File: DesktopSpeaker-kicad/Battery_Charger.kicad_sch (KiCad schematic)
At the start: 22 parts, among them J5 1S_PACK_3PIN, Q100 2N7002, SW100 WAKE_QON, SW101 BAT_DISCONNECT, U4 BQ25895RTWR

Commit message: Checkpoint isolated BQ25792/TPS25730D/TPS2116 candidates, Q100 metadata and tool wrappers
Co-Authored-By: Claude Sonnet 5.5 <noreply@anthropic.com>
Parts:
- Q100: LCSC (none) -> C65189; MPN (none) -> 2N7002,215; Manufacturer (none) -> Nexperia
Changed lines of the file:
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@@
 (wire (pts (xy 181.61 217.17) (xy 217.83 217.17)) (stroke (width 0) (type default)))
 (wire (pts (xy 217.83 217.17) (xy 217.83 205.42)) (stroke (width 0) (type default)))
-(symbol (lib_id "2N7002:2N7002") (at 173.99 232.41 0) (unit 1) (exclude_from_sim no) (in_bom yes) (on_board yes) (dnp no) (property "Reference" "Q100" (at 182.88 231.14 0) (effects (font (size 1.27 1.27)) (justify left))) (property "Value" "2N7002" (at 182.88 233.68 0) (effects (font (size 1.27 1.27)) (justify left))) (property "Footprint" "DesktopSpeaker:2N7002" (at 173.99 232.41 0) (effects (font (size 1.0 1.0)) (hide yes))) (pin "1") (pin "2") (pin "3") (instances (project "DesktopSpeaker" (path "/feda53ed-537d-4f88-9436-c6075776255b/a7066d55-4393-49f1-9dcb-c2e9f1db9549" (reference "Q100") (unit 1)))))
+(symbol (lib_id "2N7002:2N7002") (at 173.99 232.41 0) (unit 1) (exclude_from_sim no) (in_bom yes) (on_board yes) (dnp no) (property "Reference" "Q100" (at 182.88 231.14 0) (effects (font (size 1.27 1.27)) (justify left))) (property "Value" "2N7002" (at 182.88 233.68 0) (effects (font (size 1.27 1.27)) (justify left))) (property "Footprint" "DesktopSpeaker:2N7002" (at 173.99 232.41 0) (effects (font (size 1.0 1.0)) (hide yes))) (pin "1") (pin "2") (pin "3") (instances (project "DesktopSpeaker" (path "/feda53ed-537d-4f88-9436-c6075776255b/a7066d55-4393-49f1-9dcb-c2e9f1db9549" (reference "Q100") (unit 1)))) (property "MPN" "2N7002,215" (at 173.99 232.41 0) (effects (font (size 1 1)) (hide yes))) (property "Manufacturer" "Nexperia" (at 173.99 232.41 0) (effects (font (size 1 1)) (hide yes))) (property "LCSC" "C65189" (at 173.99 232.41 0) (effects (font (size 1 1)) (hide yes))))
 (wire (pts (xy 176.53 227.33) (xy 176.53 217.17)) (stroke (width 0) (type default)))
 (wire (pts (xy 176.53 217.17) (xy 181.61 217.17)) (stroke (width 0) (type default)))
@@
 (wire (pts (xy 360.68 147.32) (xy 360.68 154.94)) (stroke (width 0) (type default)))
 (junction (at 360.68 121.92) (diameter 0) (color 0 0 0 0))
-(symbol (lib_id "power:GND") (at 360.68 154.94 0) (unit 1) (exclude_from_sim no) (in_bom no) (on_board no) (dnp no) (property "Reference" "#PWR299" (at 365.76 153.67 0) (effects (font (size 1.27 1.27)) (justify left) (hide yes))) (property "Value" "GND" (at 365.76 156.21 0) (effects (font (size 1.27 1.27)) (justify left))) (property "Footprint" "" (at 360.68 154.94 0) (effects (font (size 1.0 1.0)) (hide yes))) (pin "1") (instances (project "DesktopSpeaker" (path "/feda53ed-537d-4f88-9436-c6075776255b/a7066d55-4393-49f1-9dcb-c2e9f1db9549" (reference "#PWR299") (unit 1))))))
+(symbol (lib_id "power:GND") (at 360.68 154.94 0) (unit 1) (exclude_from_sim no) (in_bom no) (on_board no) (dnp no) (property "Reference" "#PWR299" (at 365.76 153.67 0) (effects (font (size 1.27 1.27)) (justify left) (hide yes))) (property "Value" "GND" (at 365.76 156.21 0) (effects (font (size 1.27 1.27)) (justify left))) (property "Footprint" "" (at 360.68 154.94 0) (effects (font (size 1.0 1.0)) (hide yes))) (pin "1") (instances (project "DesktopSpeaker" (path "/feda53ed-537d-4f88-9436-c6075776255b/a7066d55-4393-49f1-9dcb-c2e9f1db9549" (reference "#PWR299") (unit 1)))))
+)

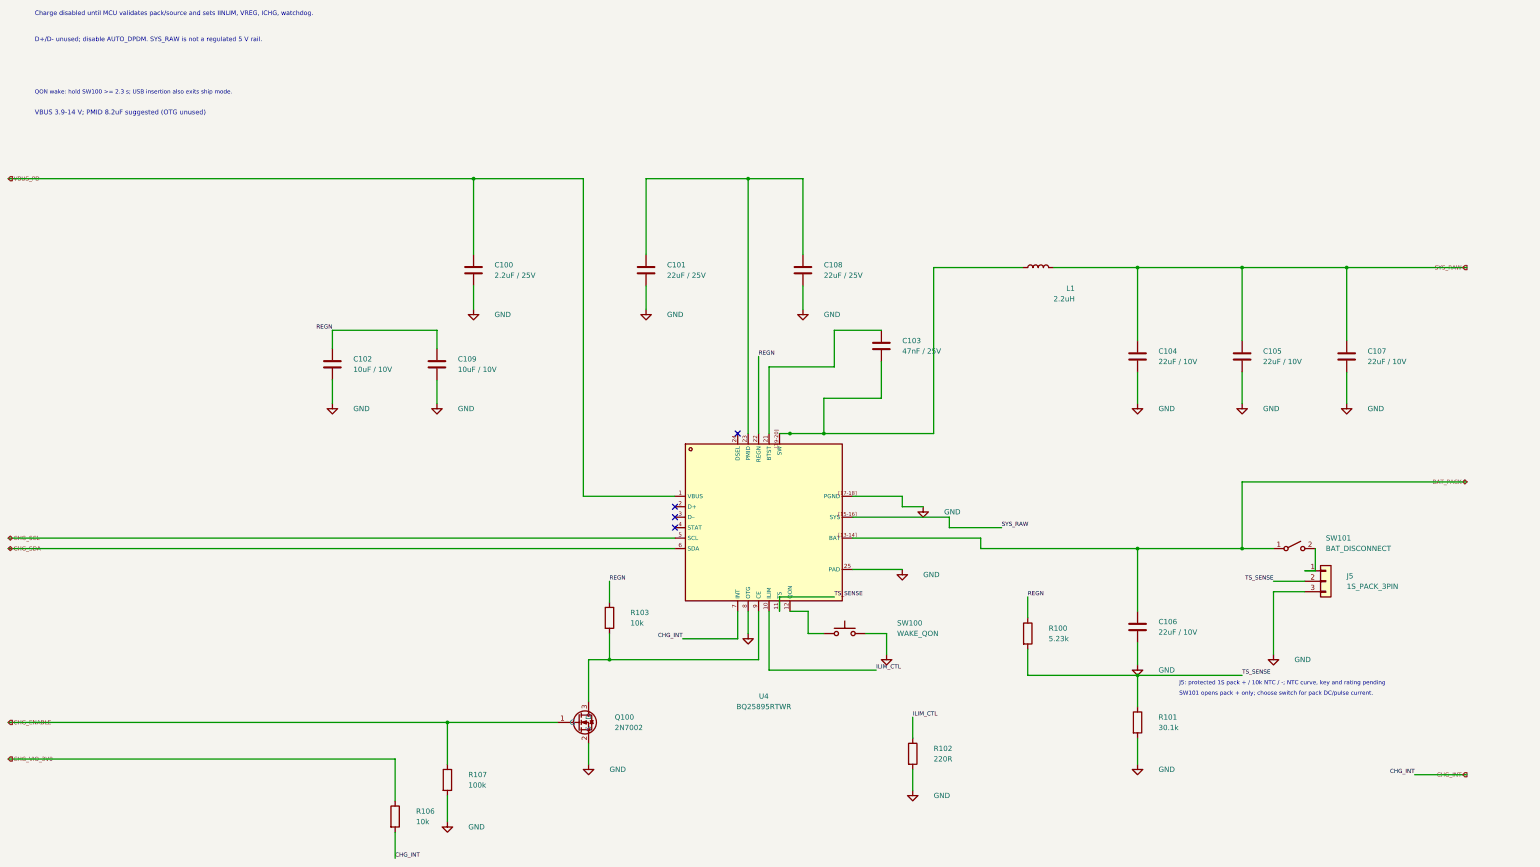
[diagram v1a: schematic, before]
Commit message: Integrate TPS25730D PD and BQ25792 charger into active project (5-20 V); update BOM, plan, handover, preview
Co-Authored-By: Claude Sonnet 5.5 <noreply@anthropic.com>
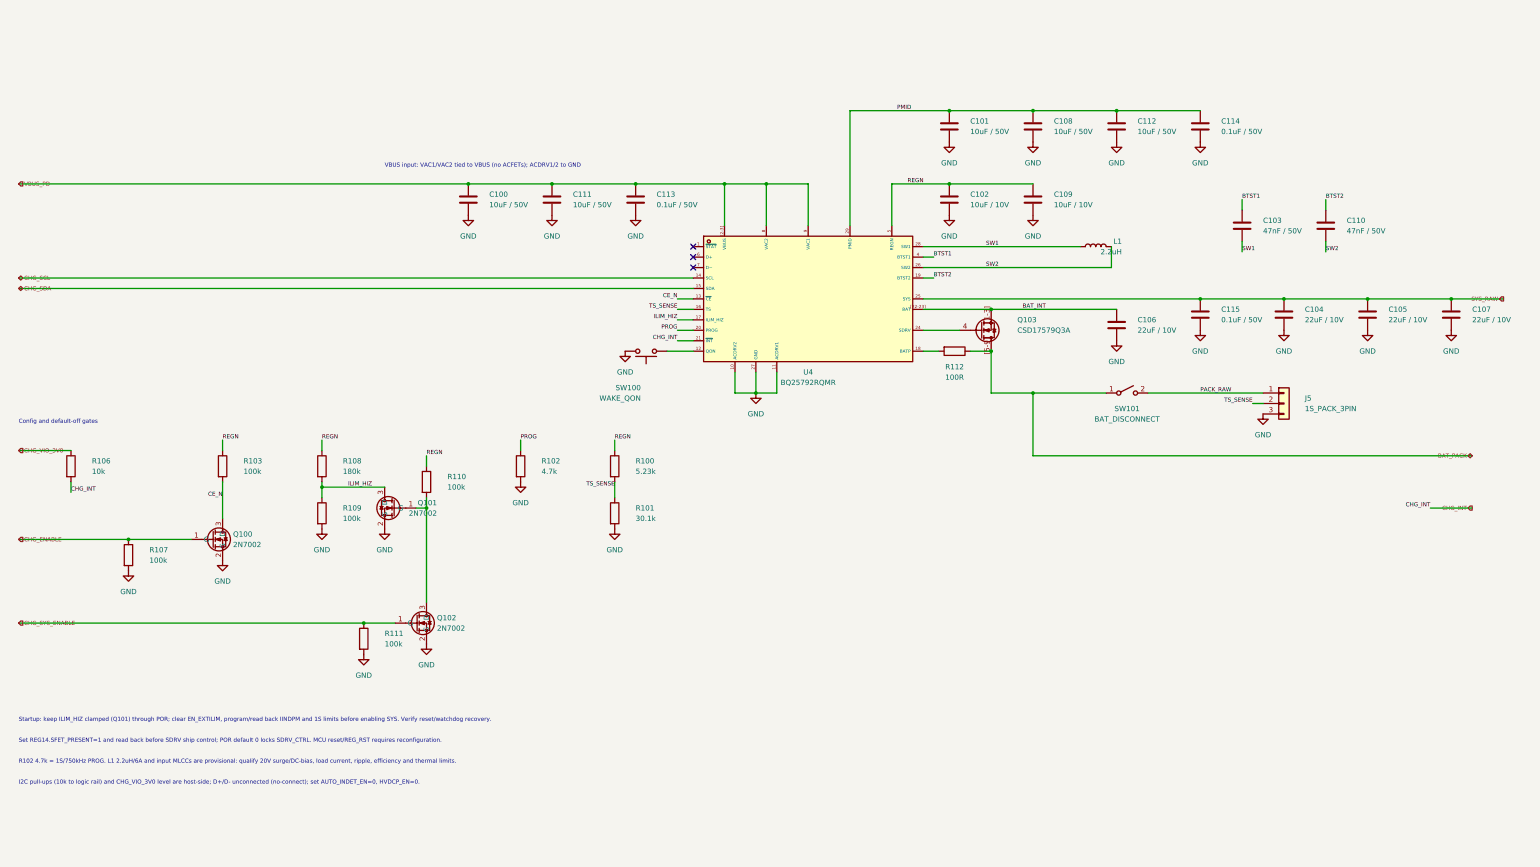
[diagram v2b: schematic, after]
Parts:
- added C110: 47nF / 50V, DesktopSpeaker:PD_C_0603, symbol PD_C:PD_C
- added C111, C112: 10uF / 50V, DesktopSpeaker:PD_C_1210, symbol PD_C:PD_C
- added C113, C114, C115: 0.1uF / 50V, DesktopSpeaker:PD_C_0402, symbol PD_C:PD_C
- added Q101, Q102: 2N7002, DesktopSpeaker:2N7002, symbol 2N7002:2N7002
- added Q103: CSD17579Q3A, DesktopSpeaker:CSD17579Q3A_DNH0008A, symbol CSD17579Q3A:CSD17579Q3A
- added R108: 180k, DesktopSpeaker:PD_R_0603, symbol PD_R:PD_R
- added R109, R110, R111: 100k, DesktopSpeaker:PD_R_0603, symbol PD_R:PD_R
- added R112: 100R, DesktopSpeaker:PD_R_0603, symbol PD_R:PD_R
- C100: value 2.2uF / 25V -> 10uF / 50V; footprint DesktopSpeaker:PD_C_0805 -> DesktopSpeaker:PD_C_1210; LCSC Part C2762602 -> C138687; MPN CL21B225KBYNNNE -> CL32B106KBJNNNE
- C101, C108: value 22uF / 25V -> 10uF / 50V; LCSC Part C309062 -> C138687; MPN CL32B226KAJNNNE -> CL32B106KBJNNNE
- C103: value 47nF / 25V -> 47nF / 50V
- Q100: LCSC C65189 -> (none); MPN 2N7002,215 -> (none); Manufacturer Nexperia -> (none)
- R102: value 220R -> 4.7k; LCSC C107696 -> C99782; MPN RC0603FR-07220RL -> RC0603FR-074K7L
- R103: value 10k -> 100k; LCSC C98220 -> C14675; MPN RC0603FR-0710KL -> RC0603FR-07100KL
- U4: value BQ25895RTWR -> BQ25792RQMR; footprint DesktopSpeaker:BQ25895RTWR -> DesktopSpeaker:BQ25792RQMR; symbol BQ25895RTWR:BQ25895RTWR -> BQ25792RQMR:BQ25792RQMR; LCSC Part C80200 -> C2862876; MPN BQ25895RTWR -> BQ25792RQMR
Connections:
- net BAT_PACK: now also Q103.[5-9] (D), R112.1; no longer C106.1, U4.[13-14] (BAT)
- net CHG_INT: now also U4.21 (~{INT}); no longer U4.7 (INT)
- net CHG_SCL: now also U4.14 (SCL); no longer U4.5 (SCL)
- net CHG_SDA: now also U4.15 (SDA); no longer U4.6 (SDA)
- net GND: now also U4.10 (ACDRV2), U4.11 (ACDRV1), U4.27 (GND), C111.2, C112.2, C113.2, C114.2, C115.2, Q101.2 (S), Q102.2 (S), R109.2, R111.2; no longer U4.25 (PAD), U4.8 (OTG), U4.[17-18] (PGND)
- net REGN: now also U4.5 (REGN), R108.1, R110.1; no longer U4.22 (REGN)
- net SYS_RAW: now also U4.25 (SYS), C115.1; no longer L1.2, U4.[15-16] (SYS)
- net TS_SENSE: now also U4.16 (TS); no longer U4.11 (TS)
- net VBUS_PD: now also U4.8 (VAC2), U4.9 (VAC1), U4.[2-3] (VBUS), C111.1, C113.1; no longer U4.1 (VBUS)
- net PMID: now reaches C101.1, C108.1
- net PMID: now also U4.29 (PMID), C112.1, C114.1; no longer U4.23 (PMID)
- net BTST1: now reaches C103.1
- net BTST1: now also U4.4 (BTST1); no longer U4.21 (BTST)
- net at U4.24 (SDRV): now also Q103.4 (G)
- net CE_N: now reaches Q100.3 (D), R103.2
- net CE_N: now also U4.13 (~{CE}); no longer U4.9 (CE)
- net SW1: now reaches C103.2, L1.1
- net SW1: now also U4.28 (SW1); no longer U4.[19-20] (SW)
- net PACK_RAW: now reaches J5.1 (Pin_1), SW101.2 (B)
- net ILIM_CTL renamed PROG
- net PROG: now also U4.20 (PROG); no longer U4.10 (ILIM)
- new net: R112.2, U4.18 (BATP)
- new net: Q101.1 (G), Q102.3 (D), R110.2
- new net BAT_INT: C106.1, Q103.[1-3] (S), U4.[22-23] (BAT)
- new net BTST2: C110.1, U4.19 (BTST2)
- new net CHG_SYS_ENABLE: Q102.1 (G), R111.1
- new net ILIM_HIZ: Q101.3 (D), R108.2, R109.1, U4.17 (ILIM_HIZ)
- new net SW2: C110.2, L1.2, U4.26 (SW2)
- no-connect marks 4 -> 3
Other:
- note added: "Config and default-off gates"
- note added: "I2C pull-ups (10k to logic rail) and CHG_VIO_3V0 level are host-side; D+/D- unconnected (no-connect); set AUTO_INDET_EN=0, HVDCP_EN=0."
- note added: "R102 4.7k = 1S/750kHz PROG. L1 2.2uH/6A and input MLCCs are provisional: qualify 20V surge/DC-bias, load current, ripple, efficiency and thermal limits."
- note added: "Set REG14.SFET_PRESENT=1 and read back before SDRV ship control; POR default 0 locks SDRV_CTRL. MCU reset/REG_RST requires reconfiguration."
- note added: "Startup: keep ILIM_HIZ clamped (Q101) through POR; clear EN_EXTILIM, program/read back IINDPM and 1S limits before enabling SYS. Verify reset/watchdog recovery."
- note added: "VBUS input: VAC1/VAC2 tied to VBUS (no ACFETs); ACDRV1/2 to GND"
- note removed: "Charge disabled until MCU validates pack/source and sets IINLIM, VREG, ICHG, watchdog."
- note removed: "D+/D- unused; disable AUTO_DPDM. SYS_RAW is not a regulated 5 V rail."
- note removed: "J5: protected 1S pack + / 10k NTC / -; NTC curve, key and rating pending"
- note removed: "QON wake: hold SW100 >= 2.3 s; USB insertion also exits ship mode."
- note removed: "SW101 opens pack + only; choose switch for pack DC/pulse current."
- note removed: "VBUS 3.9-14 V; PMID 8.2uF suggested (OTG unused)"
- title: BQ25895 charger and 1S battery power path -> BQ25792 1S charger and power path candidate
- moved on the sheet: C100, C101, C102, C103, C104, C105, C106, C107, C108, C109, J5, L1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

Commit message: Select J5 Micro-Fit, SW100 tactile and SW101 rocker; add footprints and decisions
Co-Authored-By: Claude Sonnet 5.5 <noreply@anthropic.com>
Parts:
- J5: footprint DesktopSpeaker:JST_B3P_VH_1x03_P3.96mm_Vertical -> DesktopSpeaker:Molex_Micro-Fit_3.0_43650-0300_1x03_P3.00mm_Horizontal; LCSC (none) -> C503478; MPN (none) -> 43650-0300; Manufacturer (none) -> Molex
- SW100: footprint (none) -> DesktopSpeaker:TE_1977066-1_Tact_RA_SMD; LCSC (none) -> C2972219; MPN (none) -> 1977066-1; Manufacturer (none) -> TE Connectivity
- SW101: footprint (none) -> DesktopSpeaker:SHOUHAN_KCD1-201-R_Rocker_D20_Panel; LCSC (none) -> C5884429; MPN (none) -> KCD1-201-R; Manufacturer (none) -> SHOU HAN

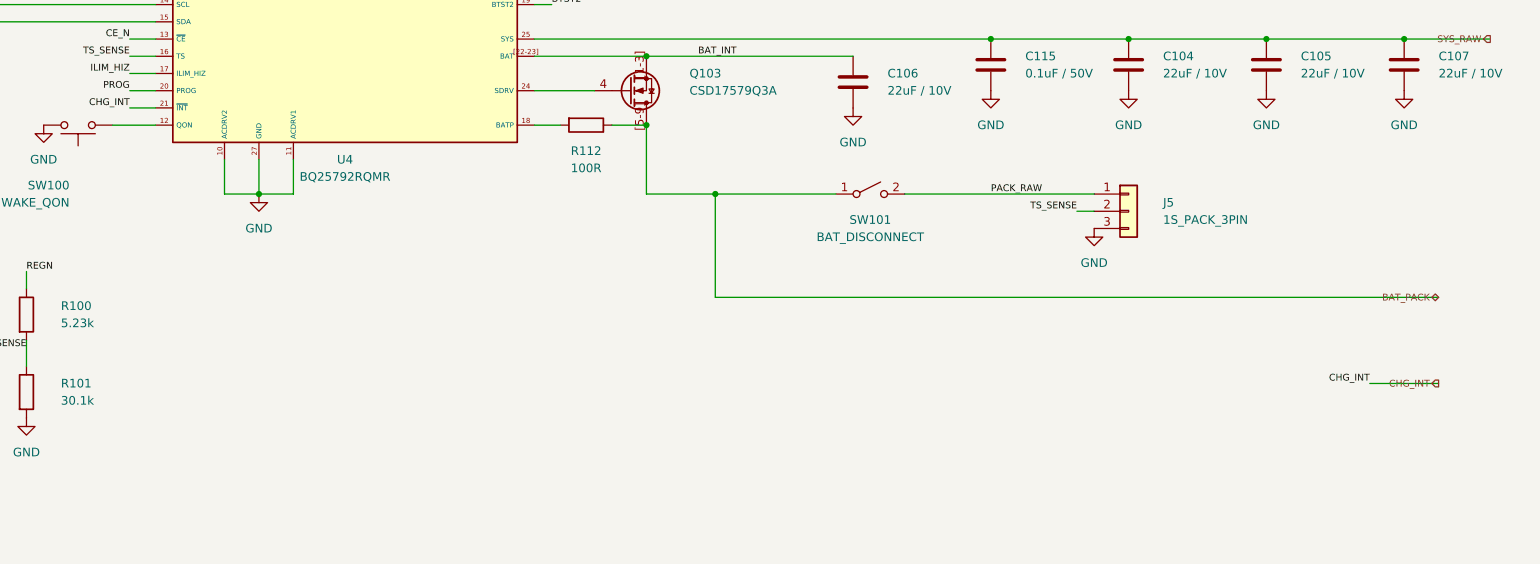
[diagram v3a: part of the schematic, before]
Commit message: Swap MCU to STM32G071RBT6; full audio-chain pin allocation and QON sense
Co-Authored-By: Claude Sonnet 5.5 <noreply@anthropic.com>
Claude-Session: https://claude.ai/code/session_01N5RHheWSjDFDPbKVD5YVeJ
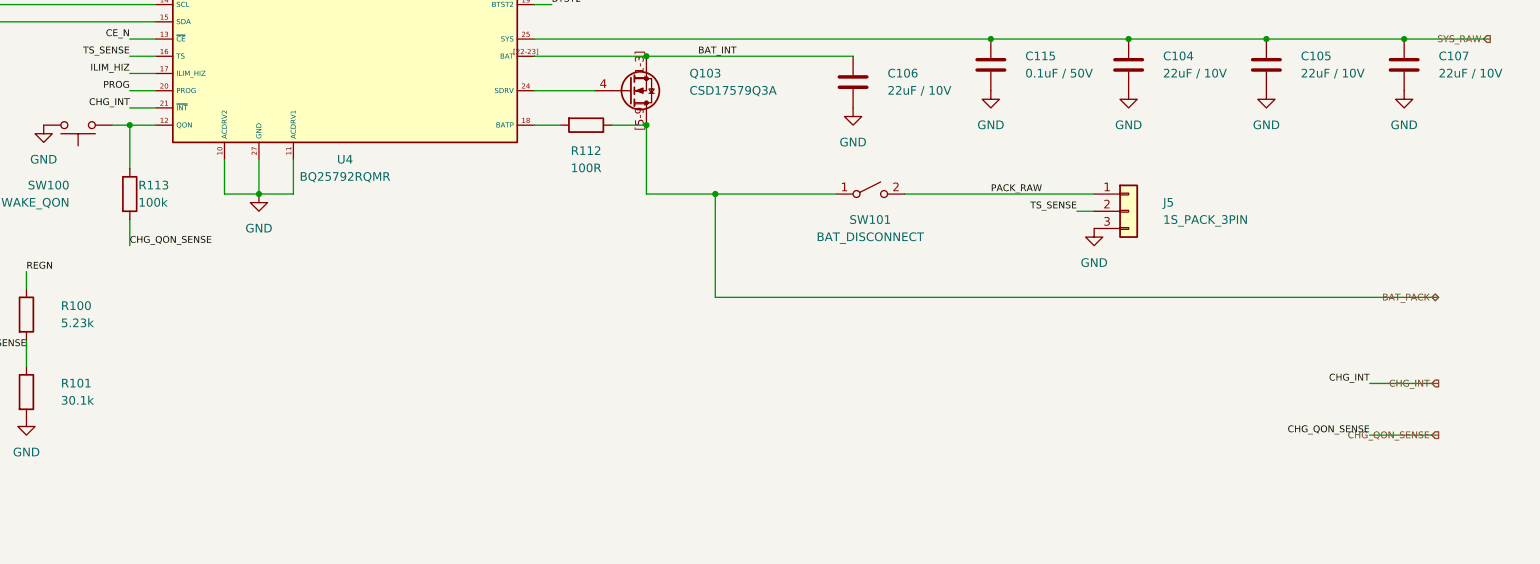
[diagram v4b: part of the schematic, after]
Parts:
- added R113: 100k, DesktopSpeaker:PD_R_0603, symbol PD_R:PD_R
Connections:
- net at SW100.1, U4.12 (QON): now also R113.1
- new net CHG_QON_SENSE: R113.2
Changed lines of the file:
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@@
 (sheet_instances (path "/" (page "1")))
 (embedded_fonts no)(wire (pts (xy 284.48 167.64) (xy 391.16 167.64)) (stroke (width 0) (type default)))
+(symbol (lib_id "PD_R:PD_R") (at 198.12 152.4 0) (unit 1) (exclude_from_sim no) (in_bom yes) (on_board yes) (dnp no) (property "Reference" "R113" (at 199.39 151.13 0) (effects (font (size 1.27 1.27)) (justify left))) (property "Value" "100k" (at 199.39 153.67 0) (effects (font (size 1.27 1.27)) (justify left))) (property "Footprint" "DesktopSpeaker:PD_R_0603" (at 198.12 152.4 0) (hide yes) (effects (font (size 1.27 1.27)))) (property "MPN" "RC0603FR-07100KL" (at 198.12 152.4 0) (hide yes) (effects (font (size 1.27 1.27)))) (property "Manufacturer" "YAGEO" (at 198.12 152.4 0) (hide yes) (effects (font (size 1 1)))) (property "LCSC" "C14675" (at 198.12 152.4 0) (hide yes) (effects (font (size 1 1)))) (property "Datasheet" "${KIPRJMOD}/../ai-files/datasheets/Yageo_RC0603FR_series.pdf" (at 198.12 152.4 0) (hide yes) (effects (font (size 1 1)))) (pin "1") (pin "2") (instances (project "DesktopSpeaker" (path "/feda53ed-537d-4f88-9436-c6075776255b/a7066d55-4393-49f1-9dcb-c2e9f1db9549" (reference "R113") (unit 1)))))
+(wire (pts (xy 198.12 142.24) (xy 198.12 148.59)) (stroke (width 0) (type default)))
+(junction (at 198.12 142.24) (diameter 0) (color 0 0 0 0))
+(wire (pts (xy 198.12 156.21) (xy 198.12 160.02)) (stroke (width 0) (type default)))
+(label "CHG_QON_SENSE" (at 198.12 160.02 0) (effects (font (size 1 1)) (justify left bottom)))
+(wire (pts (xy 381 187.96) (xy 391.16 187.96)) (stroke (width 0) (type default)))
+(label "CHG_QON_SENSE" (at 381.0 187.96 0) (effects (font (size 1 1)) (justify right bottom)))
+(hierarchical_label "CHG_QON_SENSE" (shape output) (at 391.16 187.96 0) (effects (font (size 1.0 1.0)) (justify right bottom)))
 )

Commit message: Final integration cleanup: BQ25792 symbol sync, BAT_INT/BATP flags, BOM sweep, plan and open-items list
Co-Authored-By: Claude Sonnet 5.5 <noreply@anthropic.com>
Claude-Session: https://claude.ai/code/session_01N5RHheWSjDFDPbKVD5YVeJ
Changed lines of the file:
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@@
 (text "R102 4.7k = 1S/750kHz PROG. L1 2.2uH/6A and input MLCCs are provisional: qualify 20V surge/DC-bias, load current, ripple, efficiency and thermal limits." (at 38.1 242.57 0) (effects (font (size 1.0 1.0)) (justify left bottom)))
 (text "I2C pull-ups (10k to logic rail) and CHG_VIO_3V0 level are host-side; D+/D- unconnected (no-connect); set AUTO_INDET_EN=0, HVDCP_EN=0." (at 38.1 247.65 0) (effects (font (size 1.0 1.0)) (justify left bottom)))
+(symbol (lib_id "PD_PWR_FLAG:PD_PWR_FLAG") (at 266.7 132.08 0) (unit 1) (exclude_from_sim no) (in_bom no) (on_board no) (dnp no) (property "Reference" "#FLG210" (at 266.7 125.73000000000002 0) (hide yes) (effects (font (size 1.27 1.27)))) (property "Value" "PWR_FLAG" (at 266.7 128.27 0) (hide yes) (effects (font (size 1.27 1.27)))) (property "Footprint" "" (at 266.7 132.08 0) (hide yes) (effects (font (size 1.27 1.27)))) (property "Datasheet" "" (at 266.7 132.08 0) (hide yes) (effects (font (size 1.27 1.27)))) (pin "1") (instances (project "DesktopSpeaker" (path "/feda53ed-537d-4f88-9436-c6075776255b/a7066d55-4393-49f1-9dcb-c2e9f1db9549" (reference "#FLG210") (unit 1)))))
+(junction (at 266.7 132.08) (diameter 0) (color 0 0 0 0))
+(symbol (lib_id "PD_PWR_FLAG:PD_PWR_FLAG") (at 259.08 142.24 0) (unit 1) (exclude_from_sim no) (in_bom no) (on_board no) (dnp no) (property "Reference" "#FLG211" (at 259.08 135.89 0) (hide yes) (effects (font (size 1.27 1.27)))) (property "Value" "PWR_FLAG" (at 259.08 138.43 0) (hide yes) (effects (font (size 1.27 1.27)))) (property "Footprint" "" (at 259.08 142.24 0) (hide yes) (effects (font (size 1.27 1.27)))) (property "Datasheet" "" (at 259.08 142.24 0) (hide yes) (effects (font (size 1.27 1.27)))) (pin "1") (instances (project "DesktopSpeaker" (path "/feda53ed-537d-4f88-9436-c6075776255b/a7066d55-4393-49f1-9dcb-c2e9f1db9549" (reference "#FLG211") (unit 1)))))
+(junction (at 259.08 142.24) (diameter 0) (color 0 0 0 0))
 (sheet_instances (path "/" (page "1")))
 (embedded_fonts no)(wire (pts (xy 284.48 167.64) (xy 391.16 167.64)) (stroke (width 0) (type default)))
